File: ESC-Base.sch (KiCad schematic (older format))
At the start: 31 parts

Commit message: Layout begonnen
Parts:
- removed F? (x2): FUSE, symbol FUSE
- removed P? (x2): CONN_01X04, symbol CONN_01X04
- added C1: 10µ, Capacitors_SMD:C_0805_HandSoldering, symbol C
- added C2, C3: 100n, Capacitors_SMD:C_0805_HandSoldering, symbol C
- added C4: 33µ, Capacitors_SMD:c_elec_5x5.8, symbol CP
- added D1: D, Diodes_SMD:SOD-123, symbol D
- added P8: CONN_01X02, Socket_Strips:Socket_Strip_Straight_1x02, symbol CONN_01X02
- added R1: 10, Resistors_SMD:R_0603_HandSoldering, symbol R
- added U1: LM1084IS-5.0/NOPB, toni:SOT223_GND_VO_VI, symbol LM1084IS-5.0/NOPB
- C5: renamed from C?; value C -> 100n; footprint (none) -> Capacitors_SMD:C_0805_HandSoldering
- C6, C7, C8, C9: renamed from C?; footprint (none) -> Capacitors_SMD:C_0805_HandSoldering
- P1: renamed from P?; footprint (none) -> Socket_Strips:Socket_Strip_Straight_1x03
- P2, P3: renamed from P?; footprint (none) -> Socket_Strips:Socket_Strip_Straight_1x05
- P4, P5: renamed from P?; footprint (none) -> sven:PowerPole_1x2
- P6, P7: renamed from P?; footprint (none) -> sven:Pin_Header_BIG_1x04
- R10, R2, R3, R4, R5, R6, R7, R8, R9: renamed from R?; footprint (none) -> Resistors_SMD:R_0603_HandSoldering
- U2: renamed from U?; footprint (none) -> sven:POWER_SO16
- U3, U6, U7: renamed from U?; footprint DIP-4 -> sven:LTV817-Footprint
- U4, U5: renamed from U?; footprint (none) -> SMD_Packages:SOIC-8-N
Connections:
- net +5V: now also C3.1, C4.1, U1.2 (OUT)
- net GND: now also C1.2, C2.2, C3.2, C4.2, U1.1 (GND)
- net OUT1: now also U5.1 (IN), U5.2 (IN)
- net OUT2: now also U4.1 (IN), U4.2 (IN)
- net VCC: now also P8.1 (P1), P8.2 (P2), R1.2
- net Vcheck1: now reaches C7.2, P3.2 (P2), U5.8 (Vcc), U7.4
- net Vcheck2: now reaches C6.2, P2.2 (P2), U4.8 (Vcc), U6.4
- net GNDcheck1: now reaches C7.1, C9.1, P3.1 (P1), R10.2, U5.5 (GND)
- net GNDcheck2: now reaches C6.1, C8.1, P2.1 (P1), R8.2, U4.5 (GND)
- new net: C1.1, C2.1, D1.1 (K), U1.3 (IN)
- new net: D1.2 (A), R1.1
- no-connect marks 1 -> 3

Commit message: Weiter gearbeitet...
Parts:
- U3, U6, U7: footprint sven:LTV817-Footprint -> toni:SO-4
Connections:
- net OUT1: now also R9.2
- net OUT2: now also R7.2
- net at P5.2 (P2), U5.3 (OUT), U5.4 (OUT): no longer R9.2
- net at P4.2 (P2), U4.3 (OUT), U4.4 (OUT): no longer R7.2
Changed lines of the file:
@@
 F 0 "U3" H 1600 1500 50  0000 L CNN
 F 1 "LTV-817" H 1800 1500 50  0000 L CNN
-F 2 "sven:LTV817-Footprint" H 1600 1100 50  0001 L CIN
+F 2 "toni:SO-4" H 1600 1100 50  0001 L CIN
 F 3 "" H 1800 1200 50  0000 L CNN
 	1    1800 1300
@@
 F 0 "U7" H 3100 4025 50  0000 L CNN
 F 1 "LTV-817" H 3300 4025 50  0000 L CNN
-F 2 "sven:LTV817-Footprint" H 3100 3625 50  0001 L CIN
+F 2 "toni:SO-4" H 3100 3625 50  0001 L CIN
 F 3 "" H 3300 3725 50  0000 L CNN
 	1    3300 3825
@@
 	0    1    1    0
 $EndComp
-Wire Wire Line
-	2700 3725 2325 3725
-Connection ~ 2325 3725
 $Comp
 L GND #PWR010
@@
 F 0 "U6" H 6200 3975 50  0000 L CNN
 F 1 "LTV-817" H 6400 3975 50  0000 L CNN
-F 2 "sven:LTV817-Footprint" H 6200 3575 50  0001 L CIN
+F 2 "toni:SO-4" H 6200 3575 50  0001 L CIN
 F 3 "" H 6400 3675 50  0000 L CNN
 	1    6400 3775
@@
 	0    1    1    0
 $EndComp
-Wire Wire Line
-	5800 3675 5425 3675
-Connection ~ 5425 3675
 $Comp
 L GND #PWR012
@@
 Text Label 2450 3150 2    60   ~ 0
 OUT1
+Text Label 5800 3675 2    60   ~ 0
+OUT2
+Text Label 2700 3725 2    60   ~ 0
+OUT1
 $EndSCHEMATC

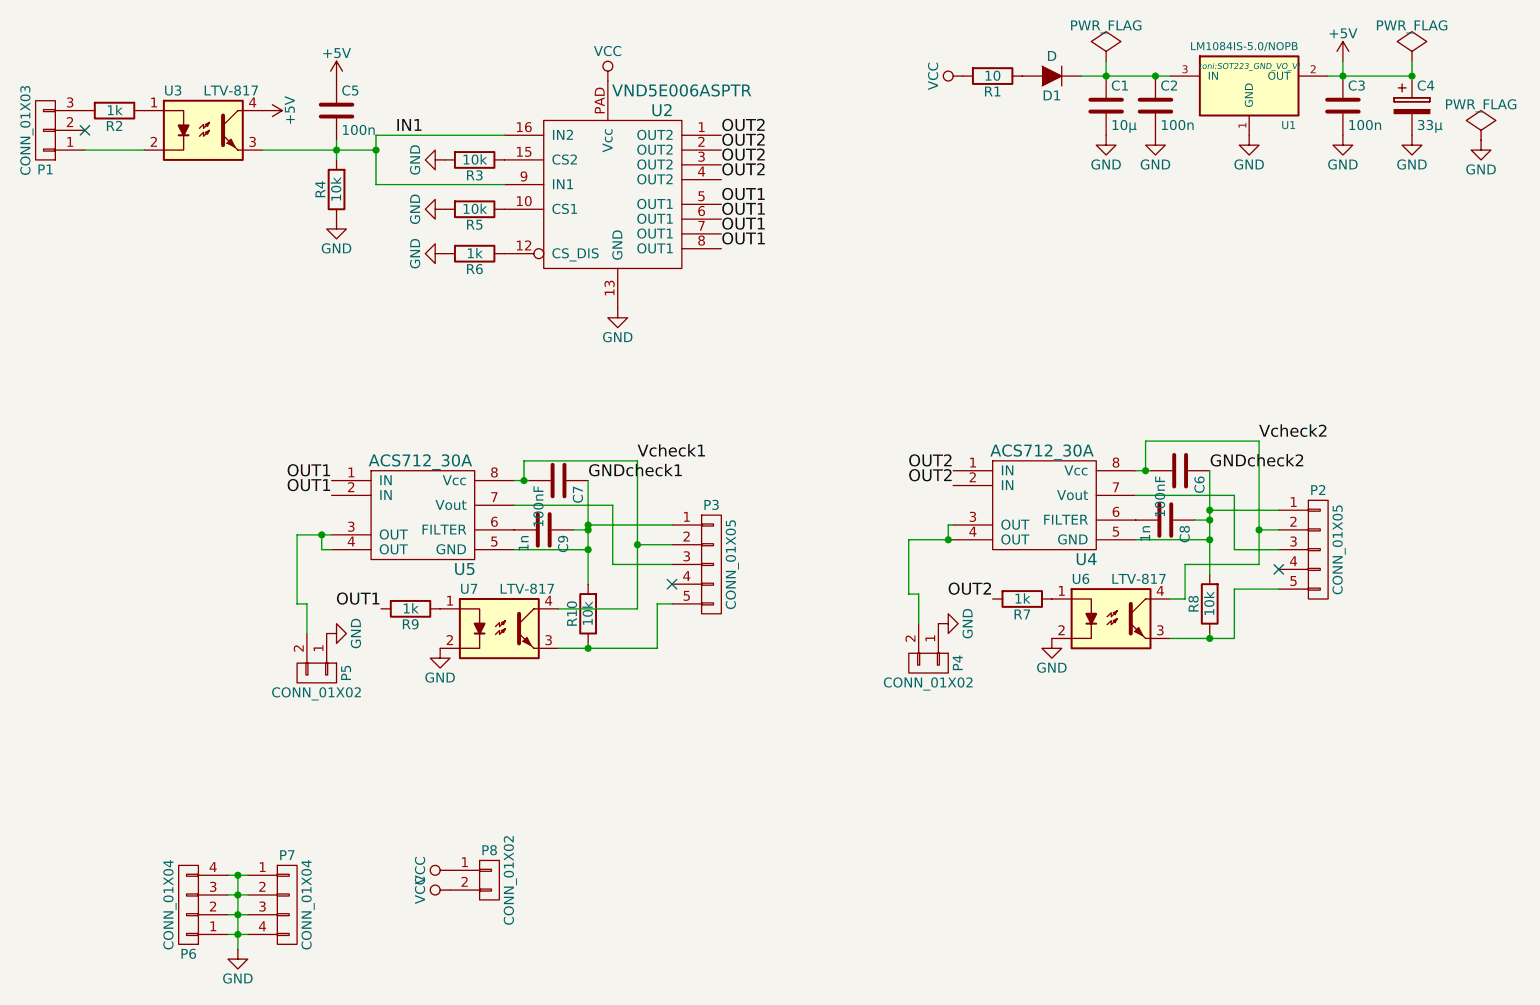
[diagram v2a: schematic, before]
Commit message: Kleinere Optimierung+Netlist-Fix
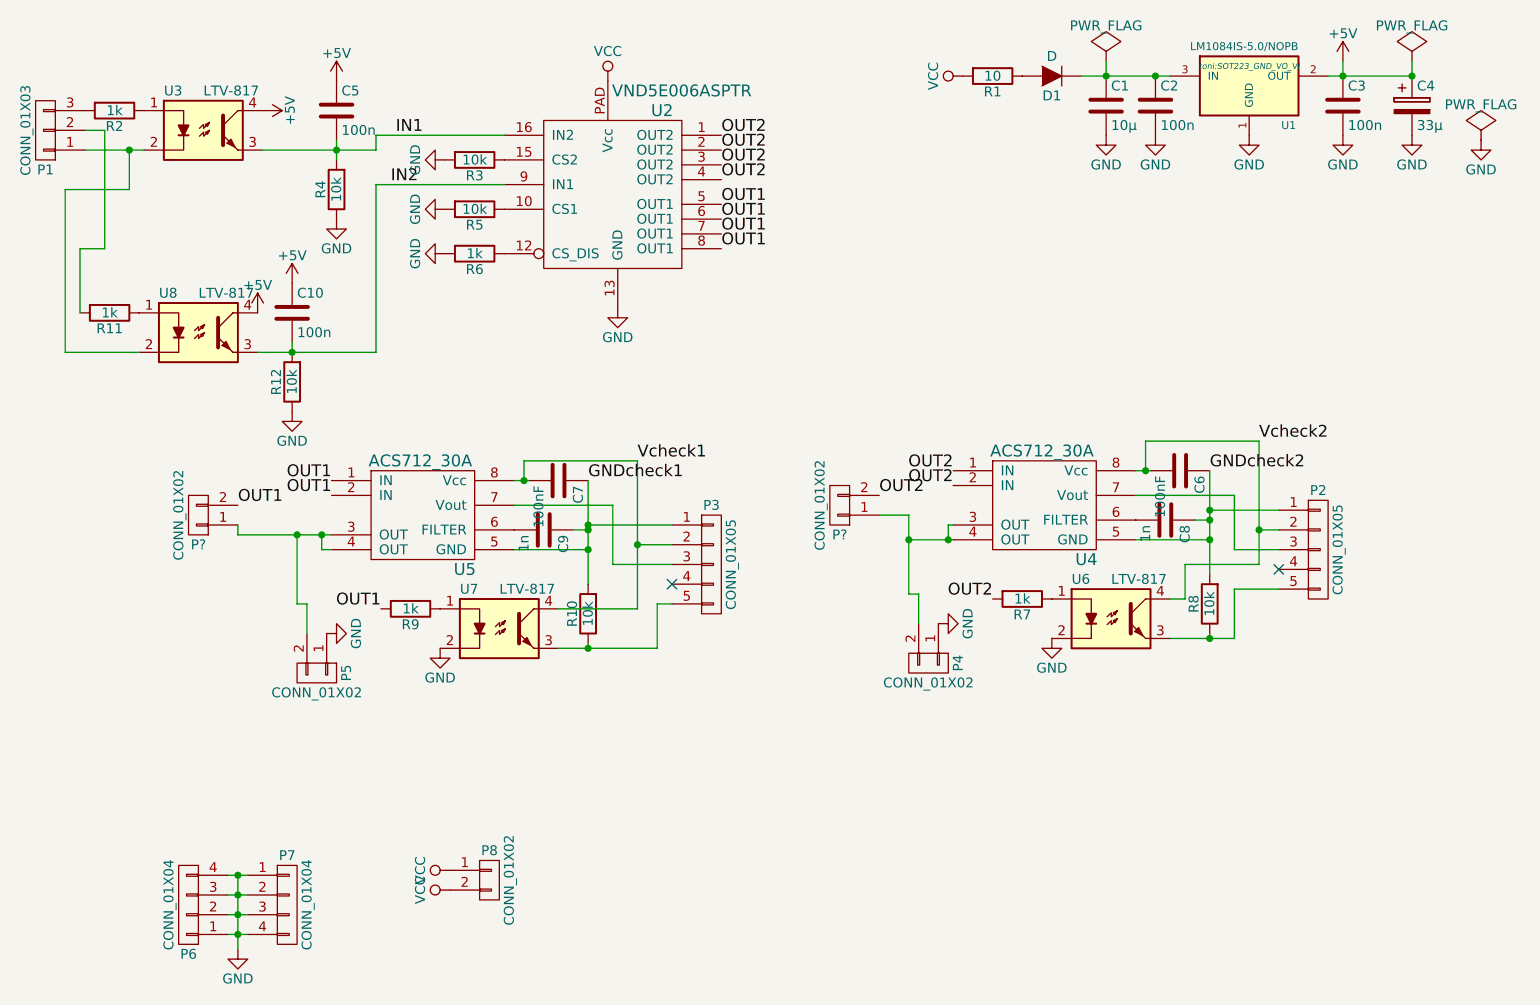
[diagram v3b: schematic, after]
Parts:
- added C10: 100n, Capacitors_SMD:C_0805_HandSoldering, symbol C
- added P? (x2): CONN_01X02, sven:PowerPole_1x2, symbol CONN_01X02
- added R11: 1k, Resistors_SMD:R_0603_HandSoldering, symbol R
- added R12: 10k, Resistors_SMD:R_0603_HandSoldering, symbol R
- added U8: LTV-817, toni:SO-4, symbol LTV-817
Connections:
- net +5V: now also C10.1, U8.4
- net GND: now also R12.1
- net IN1: no longer U2.9 (IN1)
- net OUT1: now also P?.2 (P2)
- net OUT2: now also P?.2 (P2)
- net at P5.2 (P2), U5.3 (OUT), U5.4 (OUT): now also P?.1 (P1)
- net at P1.1 (P1), U3.2: now also U8.2
- net at P1.2 (P2): now also R11.2
- net at P4.2 (P2), U4.3 (OUT), U4.4 (OUT): now also P?.1 (P1)
- new net: R11.1, U8.1
- new net IN2: C10.2, R12.2, U2.9 (IN1), U8.3
- no-connect marks 3 -> 2

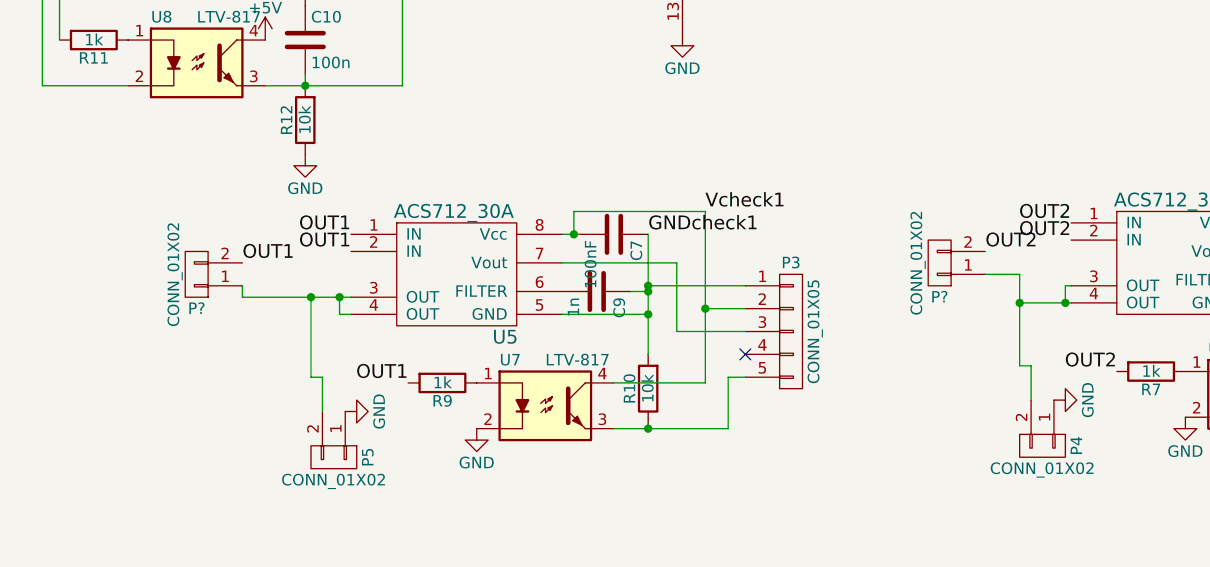
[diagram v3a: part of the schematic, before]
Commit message: Bohrungen, Lötstopplack und Bestückungsdruck: Alles Fertig!
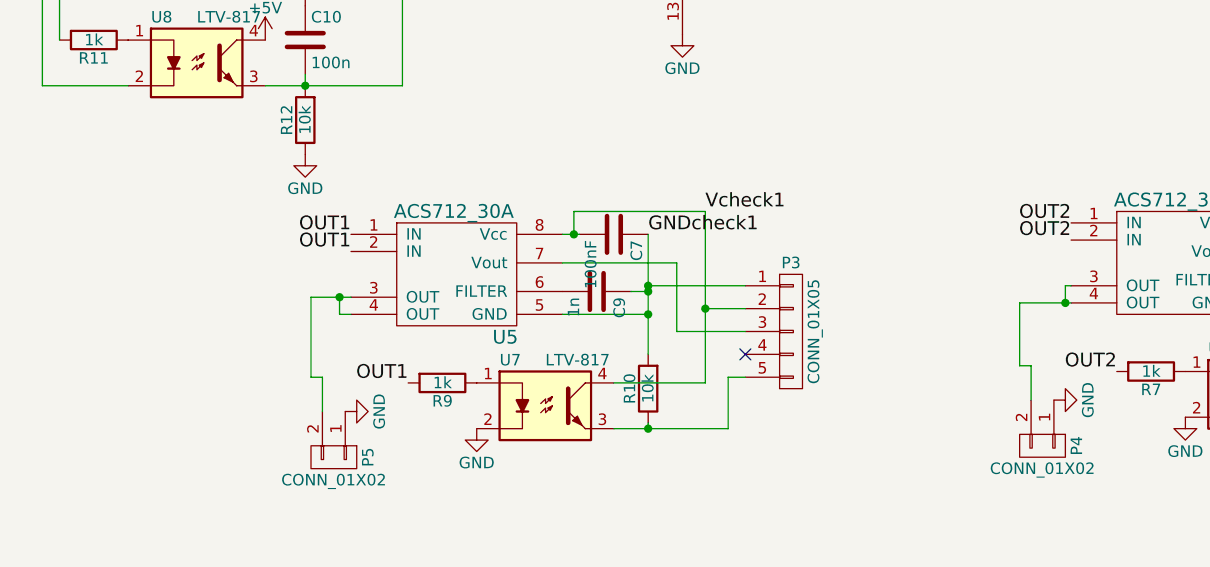
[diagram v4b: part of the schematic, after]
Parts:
- removed P? (x2): CONN_01X02, sven:PowerPole_1x2, symbol CONN_01X02
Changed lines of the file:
@@
 $EndComp
 $Comp
-L GND #PWR21
+L GND #PWR01
 U 1 1 5652C197
 P 2425 3850
-F 0 "#PWR21" H 2425 3600 50  0001 C CNN
+F 0 "#PWR01" H 2425 3600 50  0001 C CNN
 F 1 "GND" H 2425 3700 50  0000 C CNN
 F 2 "" H 2425 3850 60  0000 C CNN
@@
 	2275 3700 2275 3350
 $Comp
-L GND #PWR17
+L GND #PWR02
 U 1 1 5652C94D
 P 3900 2200
-F 0 "#PWR17" H 3900 1950 50  0001 C CNN
+F 0 "#PWR02" H 3900 1950 50  0001 C CNN
 F 1 "GND" H 3900 2050 50  0000 C CNN
 F 2 "" H 3900 2200 60  0000 C CNN
@@
 $EndComp
 $Comp
-L GND #PWR15
+L GND #PWR03
 U 1 1 5652CB59
 P 3025 1925
-F 0 "#PWR15" H 3025 1675 50  0001 C CNN
+F 0 "#PWR03" H 3025 1675 50  0001 C CNN
 F 1 "GND" H 3025 1775 50  0000 C CNN
 F 2 "" H 3025 1925 60  0000 C CNN
@@
 $EndComp
 $Comp
-L GND #PWR13
+L GND #PWR04
 U 1 1 5652D12F
 P 3025 1700
-F 0 "#PWR13" H 3025 1450 50  0001 C CNN
+F 0 "#PWR04" H 3025 1450 50  0001 C CNN
 F 1 "GND" H 3025 1550 50  0000 C CNN
 F 2 "" H 3025 1700 60  0000 C CNN
@@
 $EndComp
 $Comp
-L GND #PWR12
+L GND #PWR05
 U 1 1 5652D187
 P 3025 1450
-F 0 "#PWR12" H 3025 1200 50  0001 C CNN
+F 0 "#PWR05" H 3025 1200 50  0001 C CNN
 F 1 "GND" H 3025 1300 50  0000 C CNN
 F 2 "" H 3025 1450 60  0000 C CNN
@@
 Connection ~ 2475 1400
 $Comp
-L +5V #PWR3
+L +5V #PWR06
 U 1 1 5652D8C2
 P 2475 1050
-F 0 "#PWR3" H 2475 900 50  0001 C CNN
+F 0 "#PWR06" H 2475 900 50  0001 C CNN
 F 1 "+5V" H 2475 1190 50  0000 C CNN
 F 2 "" H 2475 1050 60  0000 C CNN
@@
 $EndComp
 $Comp
-L VCC #PWR4
+L VCC #PWR07
 U 1 1 5652D9C8
 P 3850 1050
-F 0 "#PWR4" H 3850 900 50  0001 C CNN
+F 0 "#PWR07" H 3850 900 50  0001 C CNN
 F 1 "VCC" H 3850 1200 50  0000 C CNN
 F 2 "" H 3850 1050 60  0000 C CNN
@@
 $EndComp
 $Comp
-L GND #PWR14
+L GND #PWR08
 U 1 1 5652DAB5
 P 2475 1750
-F 0 "#PWR14" H 2475 1500 50  0001 C CNN
+F 0 "#PWR08" H 2475 1500 50  0001 C CNN
 F 1 "GND" H 2475 1600 50  0000 C CNN
 F 2 "" H 2475 1750 60  0000 C CNN
@@
 $EndComp
 $Comp
-L +5V #PWR5
+L +5V #PWR09
 U 1 1 5652E85B
 P 2100 1200
-F 0 "#PWR5" H 2100 1050 50  0001 C CNN
+F 0 "#PWR09" H 2100 1050 50  0001 C CNN
 F 1 "+5V" H 2100 1340 50  0000 C CNN
 F 2 "" H 2100 1200 60  0000 C CNN
@@
 $EndComp
 $Comp
-L GND #PWR23
+L GND #PWR010
 U 1 1 5652FD02
 P 3000 3925
-F 0 "#PWR23" H 3000 3675 50  0001 C CNN
+F 0 "#PWR010" H 3000 3675 50  0001 C CNN
 F 1 "GND" H 3000 3775 50  0000 C CNN
 F 2 "" H 3000 3925 60  0000 C CNN
@@
 $EndComp
 $Comp
-L GND #PWR20
+L GND #PWR011
 U 1 1 565306B1
 P 5525 3800
-F 0 "#PWR20" H 5525 3550 50  0001 C CNN
+F 0 "#PWR011" H 5525 3550 50  0001 C CNN
 F 1 "GND" H 5525 3650 50  0000 C CNN
 F 2 "" H 5525 3800 60  0000 C CNN
@@
 	5425 3800 5425 3650
 Wire Wire Line
-	5375 3650 5425 3650
-Wire Wire Line
-	5375 3250 5375 3650
+	5425 3650 5375 3650
 $Comp
 L LTV-817 U6
@@
 $EndComp
 $Comp
-L GND #PWR22
+L GND #PWR012
 U 1 1 565306CF
 P 6100 3875
-F 0 "#PWR22" H 6100 3625 50  0001 C CNN
+F 0 "#PWR012" H 6100 3625 50  0001 C CNN
 F 1 "GND" H 6100 3725 50  0000 C CNN
 F 2 "" H 6100 3875 60  0000 C CNN
@@
 Connection ~ 1975 5375
 $Comp
-L GND #PWR26
+L GND #PWR013
 U 1 1 56537C1D
 P 1975 5450
-F 0 "#PWR26" H 1975 5200 50  0001 C CNN
+F 0 "#PWR013" H 1975 5200 50  0001 C CNN
 F 1 "GND" H 1975 5300 50  0000 C CNN
 F 2 "" H 1975 5450 60  0000 C CNN
@@
 	1    0    0    -1
 $EndComp
-Wire Wire Line
-	1975 3350 2450 3350
 Wire Wire Line
 	2450 3425 2400 3425
@@
 $EndComp
 $Comp
-L GND #PWR8
+L GND #PWR014
 U 1 1 5653A22E
 P 7100 1325
-F 0 "#PWR8" H 7100 1075 50  0001 C CNN
+F 0 "#PWR014" H 7100 1075 50  0001 C CNN
 F 1 "GND" H 7100 1175 50  0000 C CNN
 F 2 "" H 7100 1325 60  0000 C CNN
@@
 $EndComp
 $Comp
-L GND #PWR6
+L GND #PWR015
 U 1 1 5653AC4E
 P 6375 1325
-F 0 "#PWR6" H 6375 1075 50  0001 C CNN
+F 0 "#PWR015" H 6375 1075 50  0001 C CNN
 F 1 "GND" H 6375 1175 50  0000 C CNN
 F 2 "" H 6375 1325 60  0000 C CNN
@@
 $EndComp
 $Comp
-L GND #PWR7
+L GND #PWR016
 U 1 1 5653ACC5
 P 6625 1325
-F 0 "#PWR7" H 6625 1075 50  0001 C CNN
+F 0 "#PWR016" H 6625 1075 50  0001 C CNN
 F 1 "GND" H 6625 1175 50  0000 C CNN
 F 2 "" H 6625 1325 60  0000 C CNN
@@
 $EndComp
 $Comp
-L GND #PWR9
+L GND #PWR017
 U 1 1 5653AD3C
 P 7575 1325
-F 0 "#PWR9" H 7575 1075 50  0001 C CNN
+F 0 "#PWR017" H 7575 1075 50  0001 C CNN
 F 1 "GND" H 7575 1175 50  0000 C CNN
 F 2 "" H 7575 1325 60  0000 C CNN
@@
 $EndComp
 $Comp
-L GND #PWR10
+L GND #PWR018
 U 1 1 5653ADB3
 P 7925 1325
-F 0 "#PWR10" H 7925 1075 50  0001 C CNN
+F 0 "#PWR018" H 7925 1075 50  0001 C CNN
 F 1 "GND" H 7925 1175 50  0000 C CNN
 F 2 "" H 7925 1325 60  0000 C CNN
@@
 Connection ~ 6625 1025
 $Comp
-L +5V #PWR1
+L +5V #PWR019
 U 1 1 5653B22E
 P 7575 950
-F 0 "#PWR1" H 7575 800 50  0001 C CNN
+F 0 "#PWR019" H 7575 800 50  0001 C CNN
 F 1 "+5V" H 7575 1090 50  0000 C CNN
 F 2 "" H 7575 950 60  0000 C CNN
@@
 $EndComp
 $Comp
-L VCC #PWR2
+L VCC #PWR020
 U 1 1 5653B359
 P 5650 1025
-F 0 "#PWR2" H 5650 875 50  0001 C CNN
+F 0 "#PWR020" H 5650 875 50  0001 C CNN
 F 1 "VCC" H 5650 1175 50  0000 C CNN
 F 2 "" H 5650 1025 60  0000 C CNN
@@
 $EndComp
 $Comp
-L PWR_FLAG #FLG2
+L PWR_FLAG #FLG021
 U 1 1 5653B462
 P 7925 950
-F 0 "#FLG2" H 7925 1045 50  0001 C CNN
+F 0 "#FLG021" H 7925 1045 50  0001 C CNN
 F 1 "PWR_FLAG" H 7925 1130 50  0000 C CNN
 F 2 "" H 7925 950 60  0000 C CNN
@@
 $EndComp
 $Comp
-L PWR_FLAG #FLG1
+L PWR_FLAG #FLG022
 U 1 1 5653B4E0
 P 6375 950
-F 0 "#FLG1" H 6375 1045 50  0001 C CNN
+F 0 "#FLG022" H 6375 1045 50  0001 C CNN
 F 1 "PWR_FLAG" H 6375 1130 50  0000 C CNN
 F 2 "" H 6375 950 60  0000 C CNN
@@
 $EndComp
 $Comp
-L PWR_FLAG #FLG3
+L PWR_FLAG #FLG023
 U 1 1 5653B557
 P 8275 1350
-F 0 "#FLG3" H 8275 1445 50  0001 C CNN
+F 0 "#FLG023" H 8275 1445 50  0001 C CNN
 F 1 "PWR_FLAG" H 8275 1530 50  0000 C CNN
 F 2 "" H 8275 1350 60  0000 C CNN
@@
 $EndComp
 $Comp
-L GND #PWR11
+L GND #PWR024
 U 1 1 5653B5CE
 P 8275 1350
-F 0 "#PWR11" H 8275 1100 50  0001 C CNN
+F 0 "#PWR024" H 8275 1100 50  0001 C CNN
 F 1 "GND" H 8275 1200 50  0000 C CNN
 F 2 "" H 8275 1350 60  0000 C CNN
@@
 $EndComp
 $Comp
-L VCC #PWR24
+L VCC #PWR025
 U 1 1 565419E5
 P 3050 5050
-F 0 "#PWR24" H 3050 4900 50  0001 C CNN
+F 0 "#PWR025" H 3050 4900 50  0001 C CNN
 F 1 "VCC" H 3050 5200 50  0000 C CNN
 F 2 "" H 3050 5050 60  0000 C CNN
@@
 $EndComp
 $Comp
-L VCC #PWR25
+L VCC #PWR026
 U 1 1 56541B18
 P 3050 5150
-F 0 "#PWR25" H 3050 5000 50  0001 C CNN
+F 0 "#PWR026" H 3050 5000 50  0001 C CNN
 F 1 "VCC" H 3050 5300 50  0000 C CNN
 F 2 "" H 3050 5150 60  0000 C CNN
@@
 $EndComp
 $Comp
-L +5V #PWR16
+L +5V #PWR027
 U 1 1 565599AB
 P 2250 2075
-F 0 "#PWR16" H 2250 1925 50  0001 C CNN
+F 0 "#PWR027" H 2250 1925 50  0001 C CNN
 F 1 "+5V" H 2250 2215 50  0000 C CNN
 F 2 "" H 2250 2075 60  0000 C CNN
@@
 $EndComp
 $Comp
-L GND #PWR19
+L GND #PWR028
 U 1 1 56559B1D
 P 2250 2725
-F 0 "#PWR19" H 2250 2475 50  0001 C CNN
+F 0 "#PWR028" H 2250 2475 50  0001 C CNN
 F 1 "GND" H 2250 2575 50  0000 C CNN
 F 2 "" H 2250 2725 60  0000 C CNN
@@
 Connection ~ 2250 2425
 $Comp
-L +5V #PWR18
+L +5V #PWR029
 U 1 1 56559CF2
 P 2075 2225
-F 0 "#PWR18" H 2075 2075 50  0001 C CNN
+F 0 "#PWR029" H 2075 2075 50  0001 C CNN
 F 1 "+5V" H 2075 2365 50  0000 C CNN
 F 2 "" H 2075 2225 60  0000 C CNN
@@
 Text Label 2750 1575 0    60   ~ 0
 IN2
-$Comp
-L CONN_01X02 P?
-U 1 1 565D4870
-P 1775 3250
-F 0 "P?" H 1775 3400 50  0000 C CNN
-F 1 "CONN_01X02" V 1875 3250 50  0000 C CNN
-F 2 "sven:PowerPole_1x2" H 1775 3250 60  0001 C CNN
-F 3 "" H 1775 3250 60  0000 C CNN
-	1    1775 3250
-	-1   0    0    1
-$EndComp
-Wire Wire Line
-	1975 3350 1975 3300
-Connection ~ 2275 3350
-Text Label 1975 3200 0    60   ~ 0
-OUT1
-$Comp
-L CONN_01X02 P?
-U 1 1 565D4C53
-P 5025 3200
-F 0 "P?" H 5025 3350 50  0000 C CNN
-F 1 "CONN_01X02" V 5125 3200 50  0000 C CNN
-F 2 "sven:PowerPole_1x2" H 5025 3200 60  0001 C CNN
-F 3 "" H 5025 3200 60  0000 C CNN
-	1    5025 3200
-	-1   0    0    1
-$EndComp
-Text Label 5225 3150 0    60   ~ 0
-OUT2
-Wire Wire Line
-	5225 3250 5375 3250
-Connection ~ 5375 3375
+Wire Wire Line
+	5375 3650 5375 3375
+Wire Wire Line
+	2275 3350 2450 3350
 $EndSCHEMATC
